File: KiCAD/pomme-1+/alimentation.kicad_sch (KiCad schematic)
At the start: 8 parts, among them SW2 SW_SPST, T1 step down transformer, U13 LD1117V50-TO-220

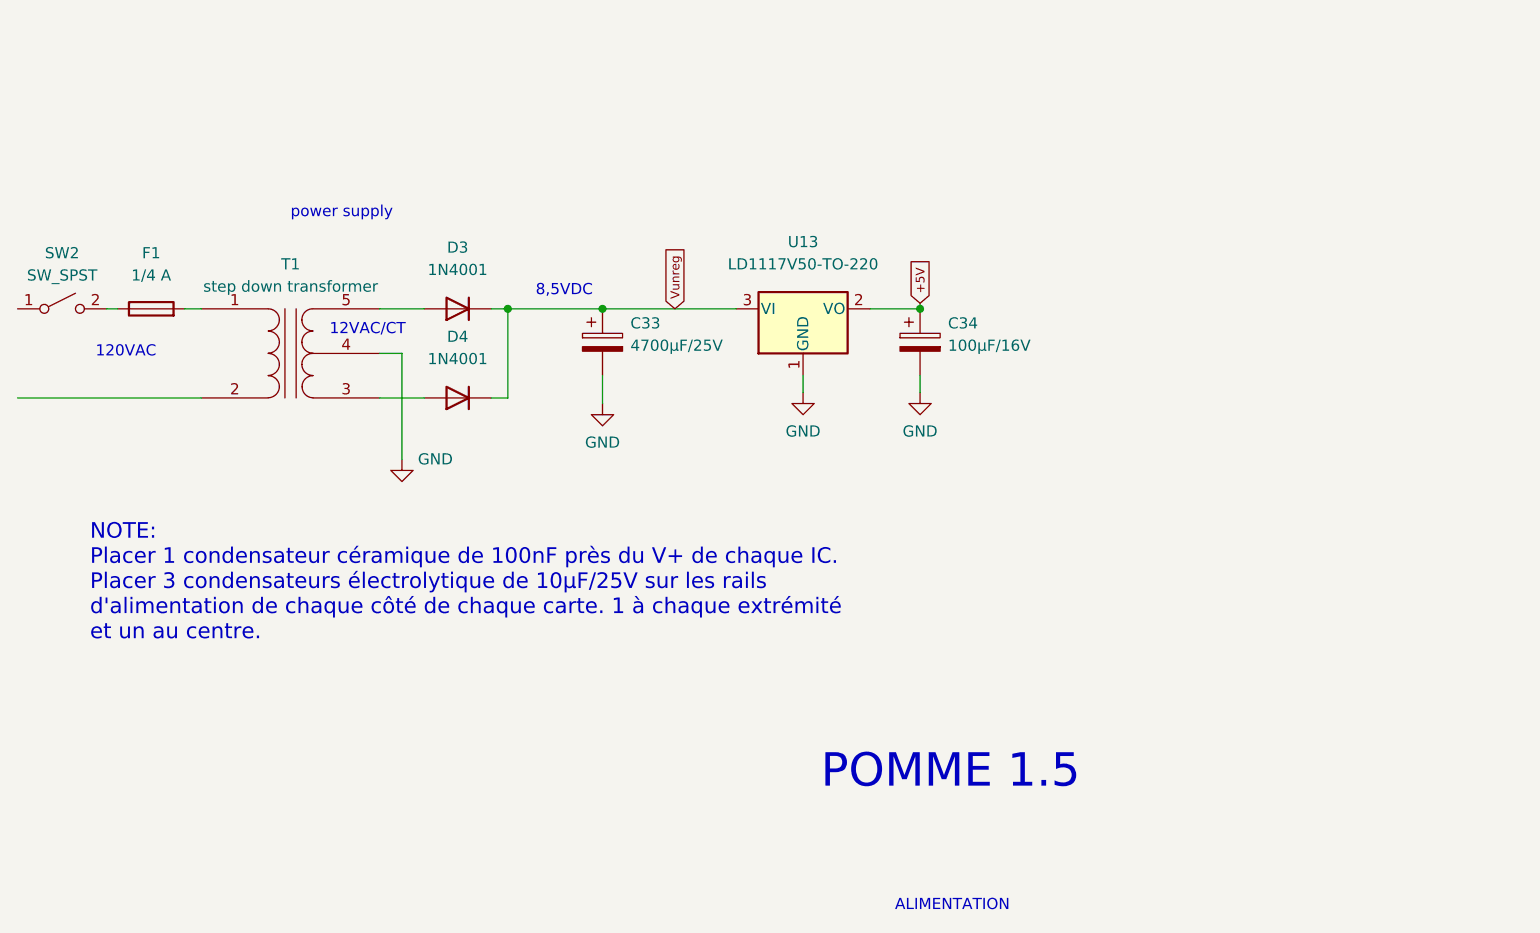
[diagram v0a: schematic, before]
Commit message: Modification de la conception du pomme 1+ Ajout d'un PIA W65C22 à la carte périphériques Ajout d'un régulateur de tension 3.3V à l'alimentation
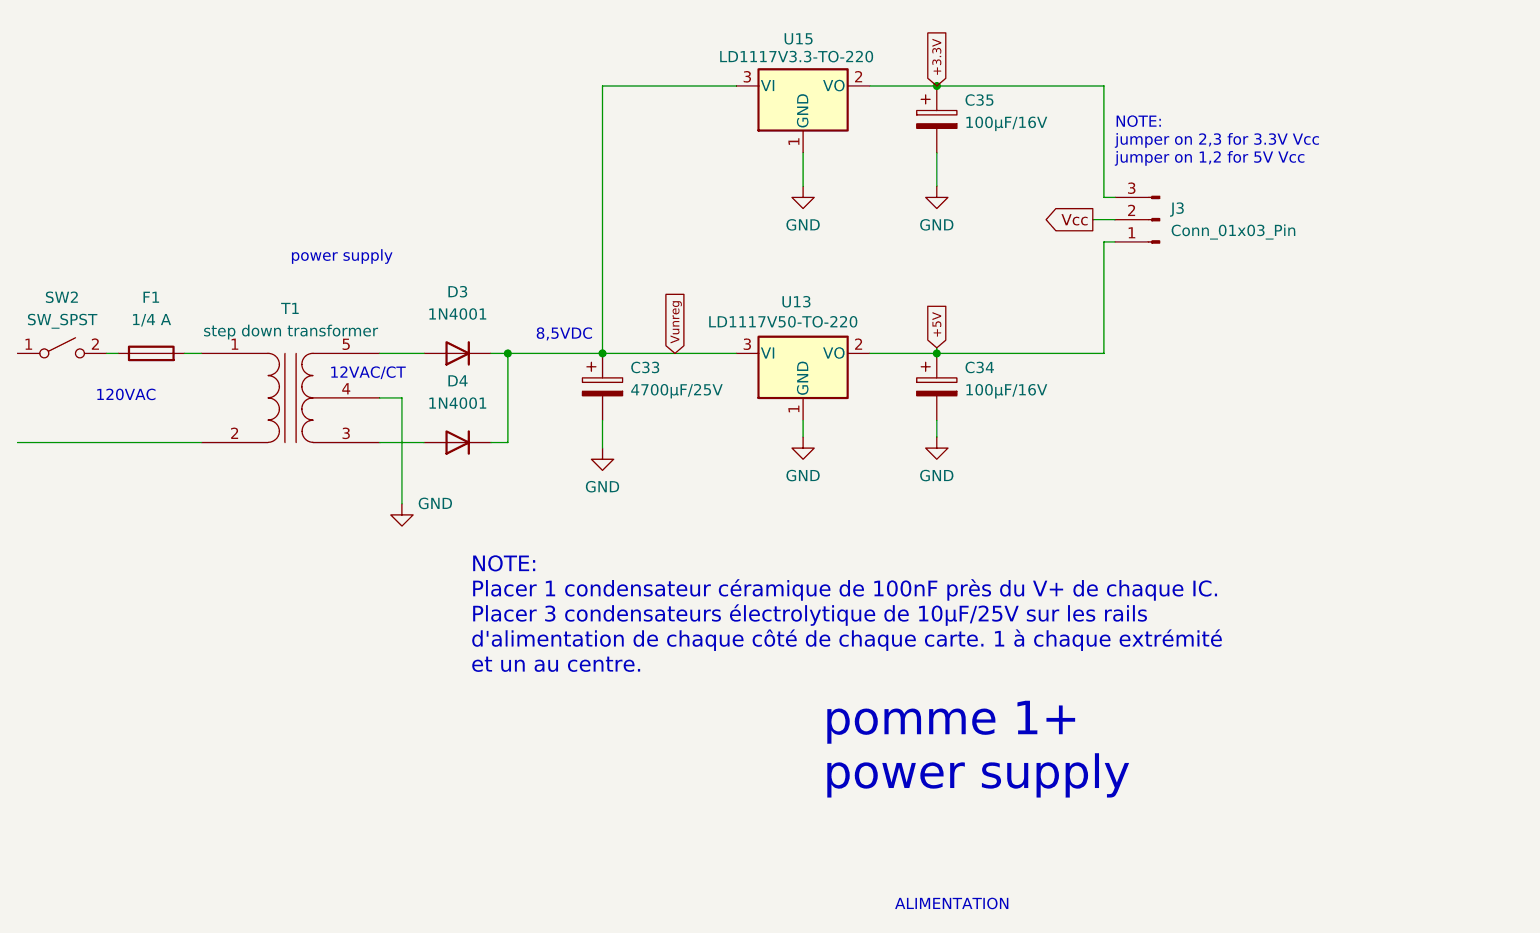
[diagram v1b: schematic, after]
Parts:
- added C35: 100µF/16V, symbol Device:C_Polarized
- added J3: Conn_01x03_Pin, symbol Connector:Conn_01x03_Pin
- added U15: LD1117V3.3-TO-220, Package_TO_SOT_SMD:SOT-223-3_TabPin2, symbol Regulator_Linear:LD1117S12TR_SOT223
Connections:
- net +5V: now also J3.1 (Pin_1)
- net GND: now also C35.2, U15.1 (GND)
- net Vunreg: now also U15.3 (VI)
- new net +3.3V: C35.1, J3.3 (Pin_3), U15.2 (VO)
- new net Vcc: J3.2 (Pin_2)
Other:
- note added: "NOTE: jumper on 2,3 for 3.3V Vcc jumper on 1,2 for 5V Vcc"
- note added: "pomme 1+ power supply"
- note removed: "POMME 1.5"
- moved on the sheet: C33, C34, D3, D4, F1, SW2, T1, U13

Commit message: Modification documents
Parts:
- renumbered C33 to C16, C35 to C17, C34 to C18, J3 to J2, U15 to U6, U13 to U7
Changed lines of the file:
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@@
 		(on_board yes)
 		(dnp no)
-		(property "Reference" "U15"
+		(property "Reference" "U6"
 			(at 176.022 91.186 0)
 			(effects
@@
 			(project "pomme-1.5"
 				(path "/46a37b86-f1f5-4cd9-9809-f219c84ab6f2/4c0c8659-beea-403b-8bf2-6163dd8a3614"
-					(reference "U15")
+					(reference "U6")
 					(unit 1)
 				)
@@
 		(on_board yes)
 		(dnp no)
-		(property "Reference" "U13"
+		(property "Reference" "U7"
 			(at 175.768 121.158 0)
 			(effects
@@
 			(project "pomme-1.5"
 				(path "/46a37b86-f1f5-4cd9-9809-f219c84ab6f2/4c0c8659-beea-403b-8bf2-6163dd8a3614"
-					(reference "U13")
+					(reference "U7")
 					(unit 1)
 				)
@@
 		(dnp no)
 		(fields_autoplaced yes)
-		(property "Reference" "#PWR027"
+		(property "Reference" "#PWR016"
 			(at 191.77 142.875 0)
 			(effects
@@
 			(project "pomme-1.5"
 				(path "/46a37b86-f1f5-4cd9-9809-f219c84ab6f2/4c0c8659-beea-403b-8bf2-6163dd8a3614"
-					(reference "#PWR027")
+					(reference "#PWR016")
 					(unit 1)
 				)
@@
 		(on_board yes)
 		(dnp no)
-		(property "Reference" "C35"
+		(property "Reference" "C17"
 			(at 194.945 98.1709 0)
 			(effects
@@
 			(project "pomme-1.5"
 				(path "/46a37b86-f1f5-4cd9-9809-f219c84ab6f2/4c0c8659-beea-403b-8bf2-6163dd8a3614"
-					(reference "C35")
+					(reference "C17")
 					(unit 1)
 				)
@@
 		(dnp no)
 		(fields_autoplaced yes)
-		(property "Reference" "#PWR030"
+		(property "Reference" "#PWR015"
 			(at 191.77 114.3 0)
 			(effects
@@
 			(project "pomme-1.5"
 				(path "/46a37b86-f1f5-4cd9-9809-f219c84ab6f2/4c0c8659-beea-403b-8bf2-6163dd8a3614"
-					(reference "#PWR030")
+					(reference "#PWR015")
 					(unit 1)
 				)
@@
 		(dnp no)
 		(fields_autoplaced yes)
-		(property "Reference" "C34"
+		(property "Reference" "C18"
 			(at 194.945 128.6509 0)
 			(effects
@@
 			(project "pomme-1.5"
 				(path "/46a37b86-f1f5-4cd9-9809-f219c84ab6f2/4c0c8659-beea-403b-8bf2-6163dd8a3614"
-					(reference "C34")
+					(reference "C18")
 					(unit 1)
 				)
@@
 		(dnp no)
 		(fields_autoplaced yes)
-		(property "Reference" "#PWR026"
+		(property "Reference" "#PWR014"
 			(at 176.53 142.875 0)
 			(effects
@@
 			(project "pomme-1.5"
 				(path "/46a37b86-f1f5-4cd9-9809-f219c84ab6f2/4c0c8659-beea-403b-8bf2-6163dd8a3614"
-					(reference "#PWR026")
+					(reference "#PWR014")
 					(unit 1)
 				)
@@
 		(dnp no)
 		(fields_autoplaced yes)
-		(property "Reference" "C33"
+		(property "Reference" "C16"
 			(at 156.845 128.6509 0)
 			(effects
@@
 			(project "pomme-1.5"
 				(path "/46a37b86-f1f5-4cd9-9809-f219c84ab6f2/4c0c8659-beea-403b-8bf2-6163dd8a3614"
-					(reference "C33")
+					(reference "C16")
 					(unit 1)
 				)
@@
 		(dnp no)
 		(fields_autoplaced yes)
-		(property "Reference" "#PWR025"
+		(property "Reference" "#PWR012"
 			(at 153.67 144.145 0)
 			(effects
@@
 			(project "pomme-1.5"
 				(path "/46a37b86-f1f5-4cd9-9809-f219c84ab6f2/4c0c8659-beea-403b-8bf2-6163dd8a3614"
-					(reference "#PWR025")
+					(reference "#PWR012")
 					(unit 1)
 				)
@@
 		(dnp no)
 		(fields_autoplaced yes)
-		(property "Reference" "J3"
+		(property "Reference" "J2"
 			(at 218.44 110.4899 0)
 			(effects
@@
 			(project ""
 				(path "/46a37b86-f1f5-4cd9-9809-f219c84ab6f2/4c0c8659-beea-403b-8bf2-6163dd8a3614"
-					(reference "J3")
+					(reference "J2")
 					(unit 1)
 				)
@@
 		(on_board yes)
 		(dnp no)
-		(property "Reference" "#PWR024"
+		(property "Reference" "#PWR011"
 			(at 130.81 150.495 0)
 			(effects
@@
 			(project "pomme-1.5"
 				(path "/46a37b86-f1f5-4cd9-9809-f219c84ab6f2/4c0c8659-beea-403b-8bf2-6163dd8a3614"
-					(reference "#PWR024")
+					(reference "#PWR011")
 					(unit 1)
 				)
@@
 		(dnp no)
 		(fields_autoplaced yes)
-		(property "Reference" "#PWR029"
+		(property "Reference" "#PWR013"
 			(at 176.53 114.3 0)
 			(effects
@@
 			(project "pomme-1.5"
 				(path "/46a37b86-f1f5-4cd9-9809-f219c84ab6f2/4c0c8659-beea-403b-8bf2-6163dd8a3614"
-					(reference "#PWR029")
-					(unit 1)
-				)
+					(reference "#PWR013")
+					(unit 1)
+				)

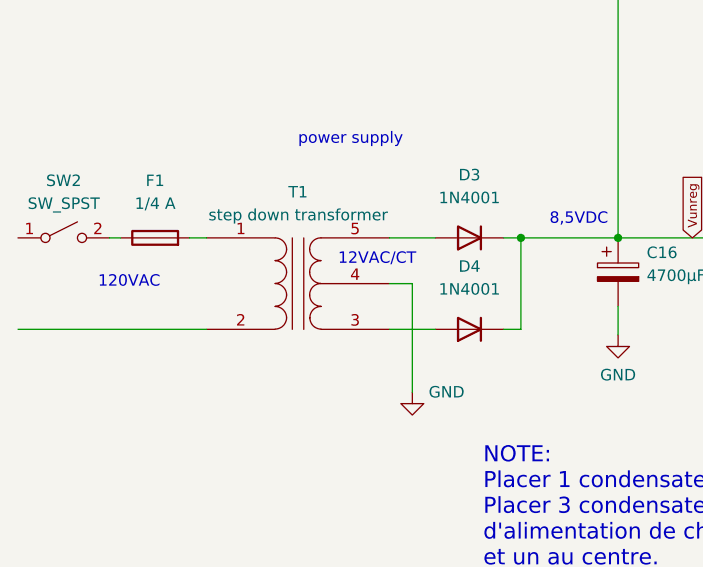
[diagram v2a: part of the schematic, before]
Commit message: Modification du circuit pour ajouter un amplificateur audio LM4861 sur la carte amovible qui se branche sur le connecteur VIA BUS
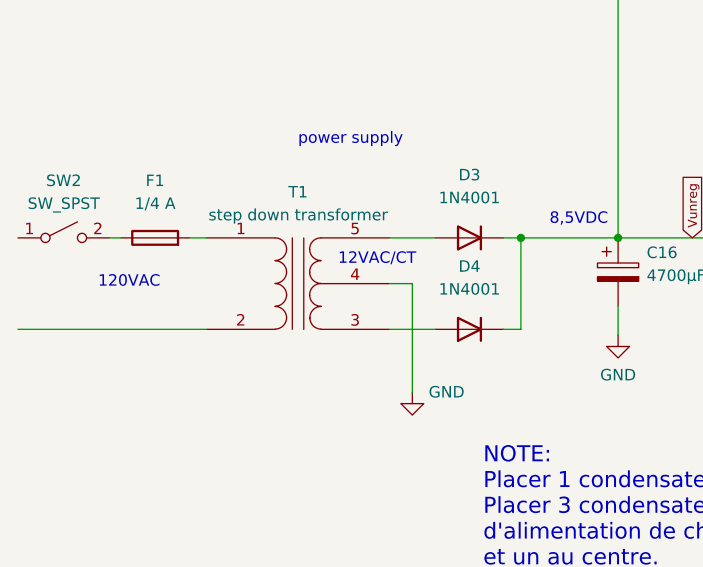
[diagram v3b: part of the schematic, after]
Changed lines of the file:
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@@
 (kicad_sch
-	(version 20231120)
+	(version 20250114)
 	(generator "eeschema")
-	(generator_version "8.0")
+	(generator_version "9.0")
 	(paper "A4")
+	(text "NOTE:\njumper on 2,3 for 3.3V Vcc\njumper on 1,2 for 5V Vcc"
+		(exclude_from_sim no)
+		(at 212.09 102.87 0)
+		(effects
+			(font
+				(size 1.27 1.27)
+			)
+			(justify left)
+		)
+	)
+	(text "120VAC"
+		(exclude_from_sim no)
+		(at 95.885 132.715 0)
+		(effects
+			(font
+				(size 1.27 1.27)
+			)
+			(justify left bottom)
+		)
+	)
+	(text "NOTE:\nPlacer 1 condensateur céramique de 100nF près du V+ de chaque IC.\nPlacer 3 condensateurs électrolytique de 10µF/25V sur les rails \nd'alimentation de chaque côté de chaque carte. 1 à chaque extrémité\net un au centre.\n"
+		(exclude_from_sim no)
+		(at 138.684 156.972 0)
+		(effects
+			(font
+				(size 1.778 1.778)
+			)
+			(justify left)
+		)
+	)
+	(text "pomme 1+\npower supply"
+		(exclude_from_sim no)
+		(at 178.816 171.958 0)
+		(effects
+			(font
+				(size 3.81 3.81)
+			)
+			(justify left)
+		)
+	)
+	(text "power supply"
+		(exclude_from_sim no)
+		(at 118.11 116.84 0)
+		(effects
+			(font
+				(size 1.27 1.27)
+			)
+			(justify left bottom)
+		)
+	)
+	(text "12VAC/CT"
+		(exclude_from_sim no)
+		(at 122.555 130.175 0)
+		(effects
+			(font
+				(size 1.27 1.27)
+			)
+			(justify left bottom)
+		)
+	)
+	(text "8,5VDC"
+		(exclude_from_sim no)
+		(at 146.05 125.73 0)
+		(effects
+			(font
+				(size 1.27 1.27)
+			)
+			(justify left bottom)
+		)
+	)
+	(text "ALIMENTATION"
+		(exclude_from_sim no)
+		(at 193.548 189.992 0)
+		(effects
+			(font
+				(size 1.27 1.27)
+			)
+		)
+	)
 	(junction
 		(at 142.875 127)
@@
 			(width 0)
 			(type default)
-		)
-	)
-	(text "NOTE:\njumper on 2,3 for 3.3V Vcc\njumper on 1,2 for 5V Vcc"
-		(exclude_from_sim no)
-		(at 212.09 102.87 0)
-		(effects
-			(font
-				(size 1.27 1.27)
-			)
-			(justify left)
-		)
-	)
-	(text "120VAC"
-		(exclude_from_sim no)
-		(at 95.885 132.715 0)
-		(effects
-			(font
-				(size 1.27 1.27)
-			)
-			(justify left bottom)
-		)
-	)
-	(text "NOTE:\nPlacer 1 condensateur céramique de 100nF près du V+ de chaque IC.\nPlacer 3 condensateurs électrolytique de 10µF/25V sur les rails \nd'alimentation de chaque côté de chaque carte. 1 à chaque extrémité\net un au centre.\n"
-		(exclude_from_sim no)
-		(at 138.684 156.972 0)
-		(effects
-			(font
-				(size 1.778 1.778)
-			)
-			(justify left)
-		)
-	)
-	(text "pomme 1+\npower supply"
-		(exclude_from_sim no)
-		(at 178.816 171.958 0)
-		(effects
-			(font
-				(size 3.81 3.81)
-			)
-			(justify left)
-		)
-	)
-	(text "power supply"
-		(exclude_from_sim no)
-		(at 118.11 116.84 0)
-		(effects
-			(font
-				(size 1.27 1.27)
-			)
-			(justify left bottom)
-		)
-	)
-	(text "12VAC/CT"
-		(exclude_from_sim no)
-		(at 122.555 130.175 0)
-		(effects
-			(font
-				(size 1.27 1.27)
-			)
-			(justify left bottom)
-		)
-	)
-	(text "8,5VDC"
-		(exclude_from_sim no)
-		(at 146.05 125.73 0)
-		(effects
-			(font
-				(size 1.27 1.27)
-			)
-			(justify left bottom)
-		)
-	)
-	(text "ALIMENTATION"
-		(exclude_from_sim no)
-		(at 193.548 189.992 0)
-		(effects
-			(font
-				(size 1.27 1.27)
-			)
 		)
 	)
@@
 		)
 	)
+	(embedded_fonts no)
 )
